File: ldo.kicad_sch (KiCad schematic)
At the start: 9 parts, among them U2 MIC5504-3.3YM5

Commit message: Resnap text to grid + add .gitignore
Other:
- company: (none) -> Tachyon PCBAs
- title: (none) -> LDO + Power Filtering
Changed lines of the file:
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@@
 	(paper "A4")
 	(title_block
-		(date "2024-09-12")
+		(title "LDO + Power Filtering")
+		(date "2024-09-15")
+		(rev "1")
+		(company "Tachyon PCBAs")
+		(comment 1 "first try surely")
 	)
 	(junction
@@
 	(text "f_{C} = 3.747kHz\n|H(f = 48kHz)| = -39.9dB"
 		(exclude_from_sim no)
-		(at 173.482 85.344 0)
+		(at 173.355 85.09 0)
 		(effects
 			(font
@@
 	(text "LDO + Input Filtering"
 		(exclude_from_sim no)
-		(at 154.432 71.374 0)
+		(at 154.305 71.12 0)
 		(effects
 			(font
@@
 	(text "f_{C} = 3.747kHz"
 		(exclude_from_sim no)
-		(at 106.68 87.63 0)
+		(at 106.68 86.995 0)
 		(effects
 			(font

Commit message: Started defining components
Man going down the capacitor dielectric rabbit hole eats up SO MUCH TIME
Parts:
- added D5: PESD3V3Y1BSF, Diode_SMD:Nexperia_DSN0603-2_0.6x0.3mm_P0.4mm, symbol Device:D_TVS
- C10, C11: footprint (none) -> Capacitor_SMD:C_1206_3216Metric_Pad1.33x1.80mm_HandSolder; Mouser Part Number (none) -> 581-TAJA105K020TNJ
- C12, C13, C8, C9: footprint (none) -> Capacitor_SMD:C_1210_3225Metric_Pad1.33x2.70mm_HandSolder; Mouser Part Number (none) -> 80-C1210C226K8R
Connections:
- net GND: now also D5.1 (A1)
- net VCC: now also D5.2 (A2)
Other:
- moved on the sheet: C10, C11, C12, C13, C8, C9, L1, L2, U2

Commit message: Fully define components
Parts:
- U2: Mouser Part Number (none) -> 998-MIC5504-3.3YM5TR
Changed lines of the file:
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@@
+			)
+		)
+		(property "Mouser Part Number" "998-MIC5504-3.3YM5TR"
+			(at 140.97 100.33 0)
+			(effects
+				(font
+					(size 1.27 1.27)
+				)
+				(hide yes)
 			)
 		)

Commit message: Add analog volume control
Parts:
- D5: Mouser Part Number (none) -> 771-PESD3V3Y1BSFYL
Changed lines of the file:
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@@
+			)
+		)
+		(property "Mouser Part Number" "771-PESD3V3Y1BSFYL"
+			(at 162.56 102.87 0)
+			(effects
+				(font
+					(size 1.27 1.27)
+				)
+				(hide yes)
 			)
 		)

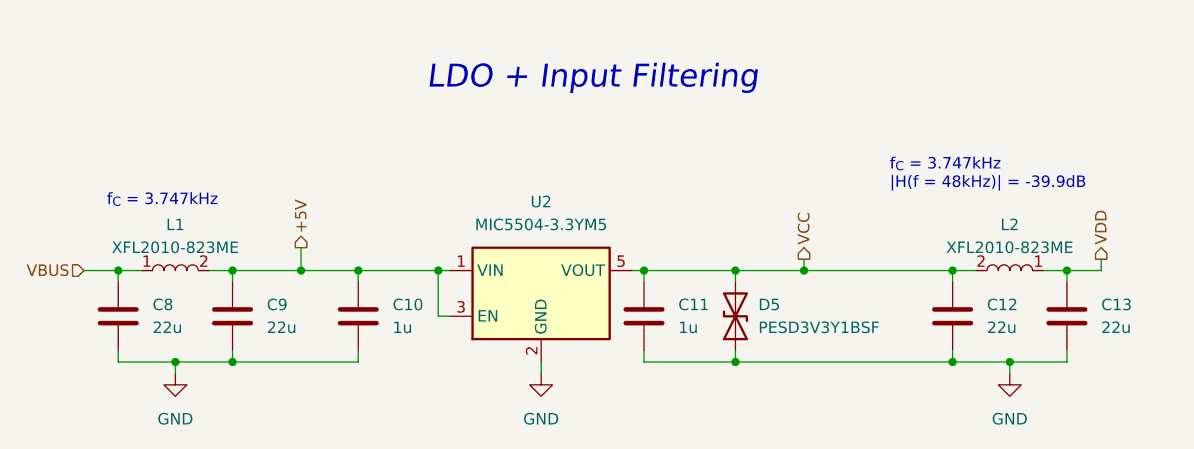
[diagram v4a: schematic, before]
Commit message: Remove potentiometer
Will have to find a different solution for volume control
Just do it OS-side?
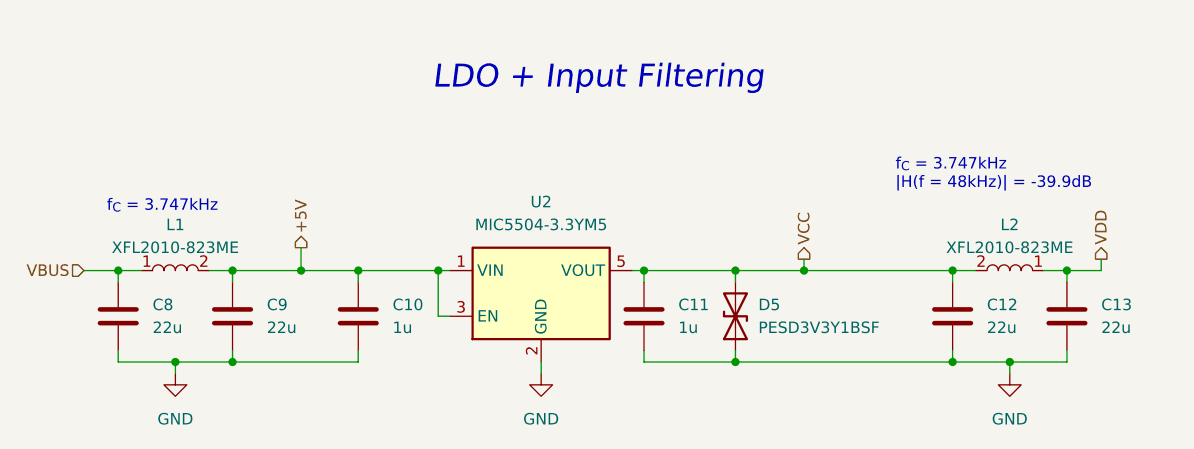
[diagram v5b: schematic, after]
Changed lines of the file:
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@@
 	(text "f_{C} = 3.747kHz\n|H(f = 48kHz)| = -39.9dB"
 		(exclude_from_sim no)
-		(at 179.705 88.9 0)
+		(at 180.34 88.9 0)
 		(effects
 			(font
@@
 	(text "LDO + Input Filtering"
 		(exclude_from_sim no)
-		(at 146.685 74.93 0)
+		(at 147.32 74.93 0)
 		(effects
 			(font
@@
 	(text "f_{C} = 3.747kHz"
 		(exclude_from_sim no)
-		(at 92.71 90.805 0)
+		(at 92.71 91.44 0)
 		(effects
 			(font

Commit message: Starting layout
Also why are the mf diodes so small
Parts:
- D5: footprint Diode_SMD:Nexperia_DSN0603-2_0.6x0.3mm_P0.4mm -> Diode_SMD:D_0201_0603Metric_Pad0.64x0.40mm_HandSolder
- renumbered C8 to C1, C9 to C2, C10 to C3, C11 to C4, C12 to C5, C13 to C6, U2 to U1
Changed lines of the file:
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@@
 		(dnp no)
 		(fields_autoplaced yes)
-		(property "Reference" "C11"
+		(property "Reference" "C4"
 			(at 156.21 101.5999 0)
 			(effects
@@
 			(project "BinauralMic"
 				(path "/d9e790b9-8aa4-4e58-8bd7-6ef4bc890627/dd5b3e13-d8cb-4f9f-b963-e8d744f036a9"
-					(reference "C11")
+					(reference "C4")
 					(unit 1)
 				)
@@
 		(on_board yes)
 		(dnp no)
-		(property "Reference" "C13"
+		(property "Reference" "C6"
 			(at 203.2 101.5999 0)
 			(effects
@@
 			(project "BinauralMic"
 				(path "/d9e790b9-8aa4-4e58-8bd7-6ef4bc890627/dd5b3e13-d8cb-4f9f-b963-e8d744f036a9"
-					(reference "C13")
+					(reference "C6")
 					(unit 1)
 				)
@@
 		(dnp no)
 		(fields_autoplaced yes)
-		(property "Reference" "U2"
+		(property "Reference" "U1"
 			(at 140.97 90.17 0)
 			(effects
@@
 			(project "BinauralMic"
 				(path "/d9e790b9-8aa4-4e58-8bd7-6ef4bc890627/dd5b3e13-d8cb-4f9f-b963-e8d744f036a9"
-					(reference "U2")
+					(reference "U1")
 					(unit 1)
 				)
@@
 		(dnp no)
 		(fields_autoplaced yes)
-		(property "Reference" "#PWR023"
+		(property "Reference" "#PWR010"
 			(at 140.97 115.57 0)
 			(effects
@@
 			(project "BinauralMic"
 				(path "/d9e790b9-8aa4-4e58-8bd7-6ef4bc890627/dd5b3e13-d8cb-4f9f-b963-e8d744f036a9"
-					(reference "#PWR023")
+					(reference "#PWR010")
 					(unit 1)
 				)
@@
 			)
 		)
-		(property "Footprint" "Diode_SMD:Nexperia_DSN0603-2_0.6x0.3mm_P0.4mm"
+		(property "Footprint" "Diode_SMD:D_0201_0603Metric_Pad0.64x0.40mm_HandSolder"
 			(at 162.56 102.87 0)
 			(effects
@@
 		(on_board yes)
 		(dnp no)
-		(property "Reference" "C12"
+		(property "Reference" "C5"
 			(at 190.5 101.5999 0)
 			(effects
@@
 			(project "BinauralMic"
 				(path "/d9e790b9-8aa4-4e58-8bd7-6ef4bc890627/dd5b3e13-d8cb-4f9f-b963-e8d744f036a9"
-					(reference "C12")
+					(reference "C5")
 					(unit 1)
 				)
@@
 		(dnp no)
 		(fields_autoplaced yes)
-		(property "Reference" "#PWR024"
+		(property "Reference" "#PWR011"
 			(at 193.04 115.57 0)
 			(effects
@@
 			(project "BinauralMic"
 				(path "/d9e790b9-8aa4-4e58-8bd7-6ef4bc890627/dd5b3e13-d8cb-4f9f-b963-e8d744f036a9"
-					(reference "#PWR024")
+					(reference "#PWR011")
 					(unit 1)
 				)
@@
 		(dnp no)
 		(fields_autoplaced yes)
-		(property "Reference" "C8"
+		(property "Reference" "C1"
 			(at 97.79 101.5999 0)
 			(effects
@@
 			(project "BinauralMic"
 				(path "/d9e790b9-8aa4-4e58-8bd7-6ef4bc890627/dd5b3e13-d8cb-4f9f-b963-e8d744f036a9"
-					(reference "C8")
+					(reference "C1")
 					(unit 1)
 				)
@@
 		(dnp no)
 		(fields_autoplaced yes)
-		(property "Reference" "#PWR015"
+		(property "Reference" "#PWR09"
 			(at 100.33 115.57 0)
 			(effects
@@
 			(project "BinauralMic"
 				(path "/d9e790b9-8aa4-4e58-8bd7-6ef4bc890627/dd5b3e13-d8cb-4f9f-b963-e8d744f036a9"
-					(reference "#PWR015")
+					(reference "#PWR09")
 					(unit 1)
 				)
@@
 		(on_board yes)
 		(dnp no)
-		(property "Reference" "C9"
+		(property "Reference" "C2"
 			(at 110.49 101.5999 0)
 			(effects
@@
 			(project "BinauralMic"
 				(path "/d9e790b9-8aa4-4e58-8bd7-6ef4bc890627/dd5b3e13-d8cb-4f9f-b963-e8d744f036a9"
-					(reference "C9")
+					(reference "C2")
 					(unit 1)
 				)
@@
 		(dnp no)
 		(fields_autoplaced yes)
-		(property "Reference" "C10"
+		(property "Reference" "C3"
 			(at 124.46 101.5999 0)
 			(effects
@@
 			(project "BinauralMic"
 				(path "/d9e790b9-8aa4-4e58-8bd7-6ef4bc890627/dd5b3e13-d8cb-4f9f-b963-e8d744f036a9"
-					(reference "C10")
-					(unit 1)
-				)
+					(reference "C3")
+					(unit 1)
+				)

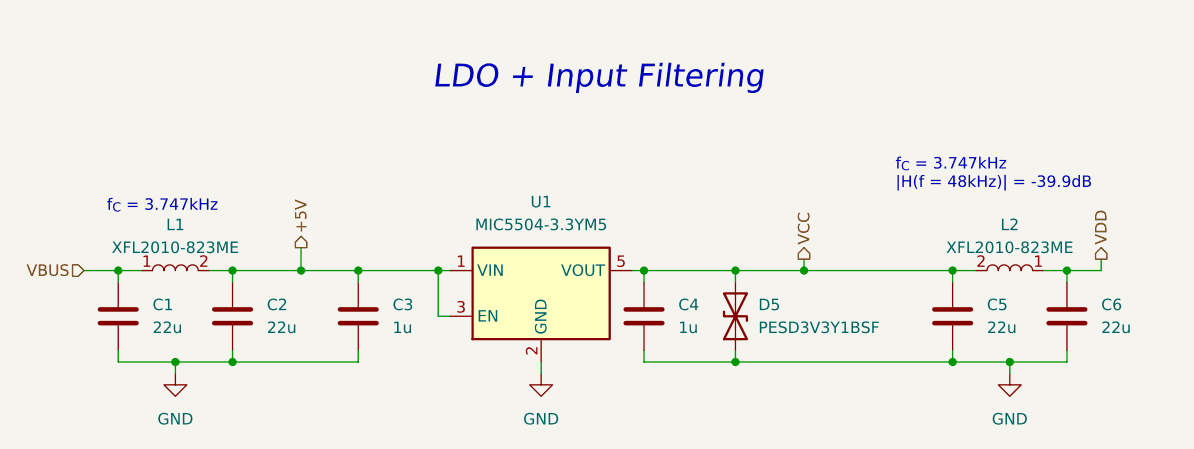
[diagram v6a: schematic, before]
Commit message: Replace 0201 diodes with recommended arrays and nothing (some were spurious and I think I don't need them)
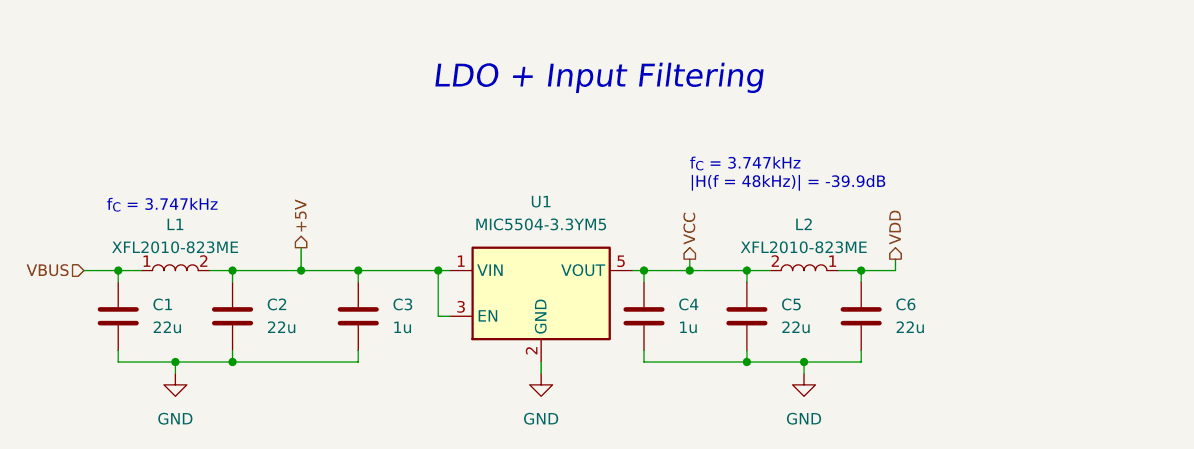
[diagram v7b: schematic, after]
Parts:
- removed D5: PESD3V3Y1BSF, Diode_SMD:D_0201_0603Metric_Pad0.64x0.40mm_HandSolder, symbol Device:D_TVS
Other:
- moved on the sheet: C5, C6, L2
